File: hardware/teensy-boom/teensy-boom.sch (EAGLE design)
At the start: 5 parts

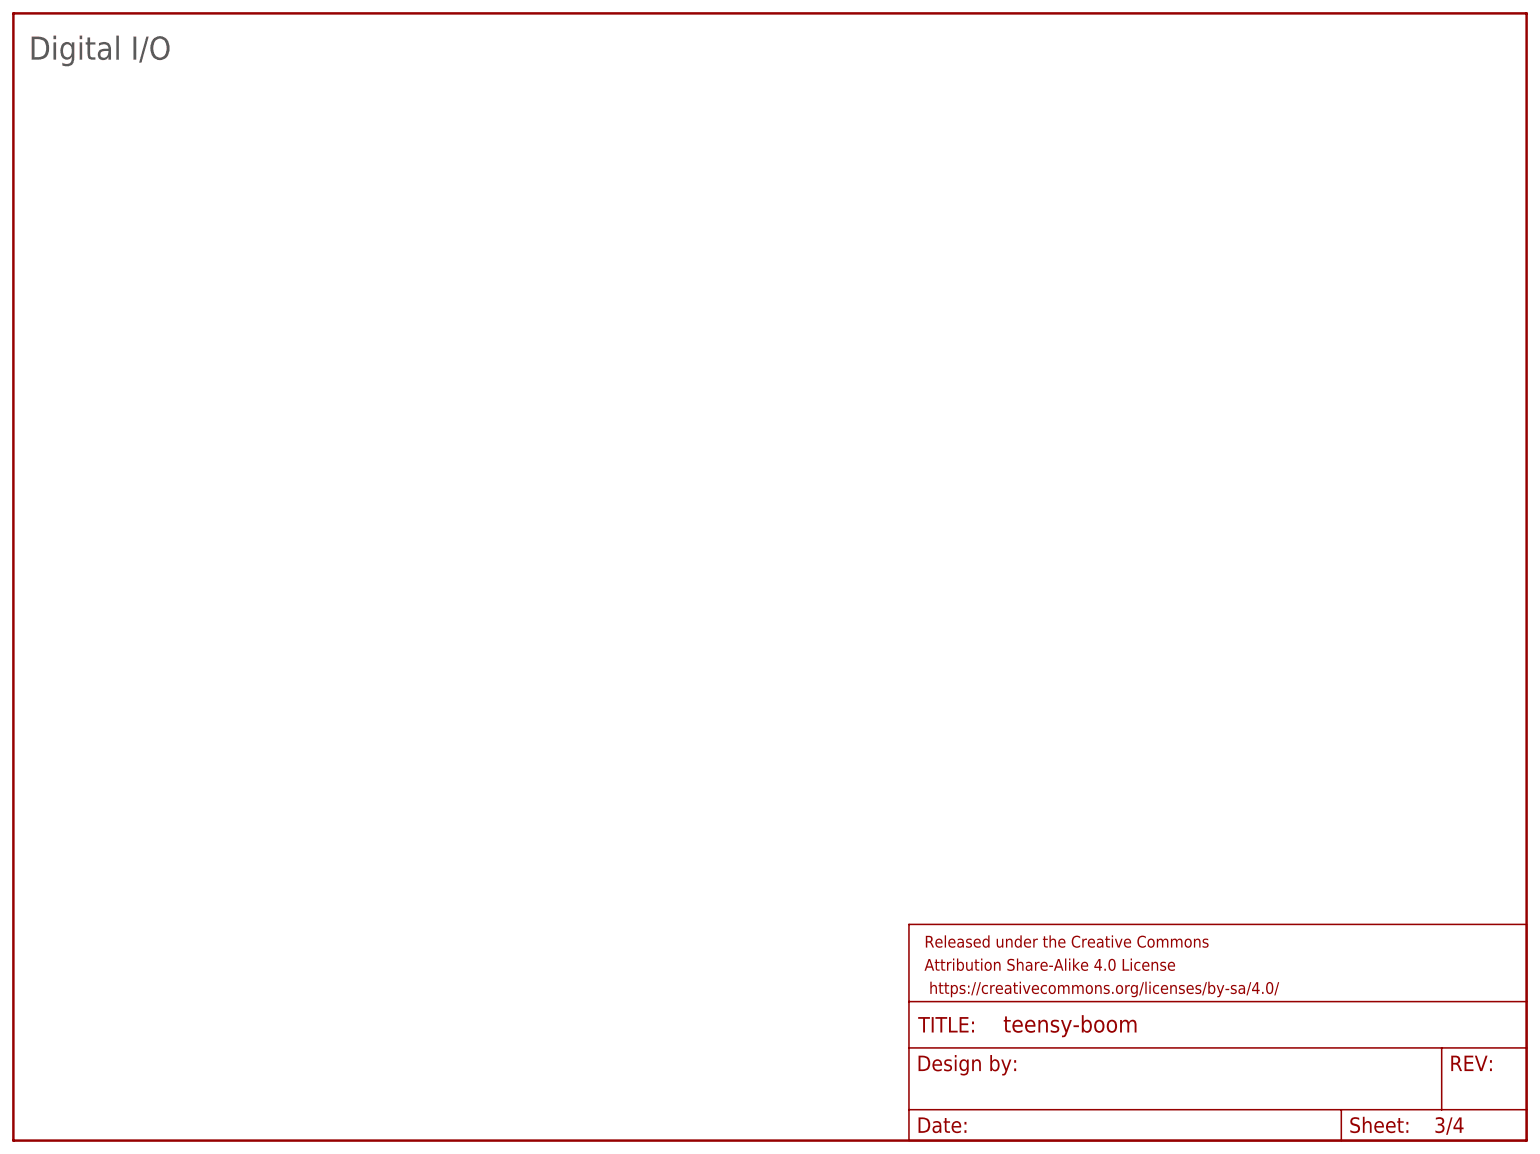
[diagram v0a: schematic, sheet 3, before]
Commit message: More PCB work
Added knobs, buttons, connectors, MIDI.

Basic PCB alignment in place...~6"x4"
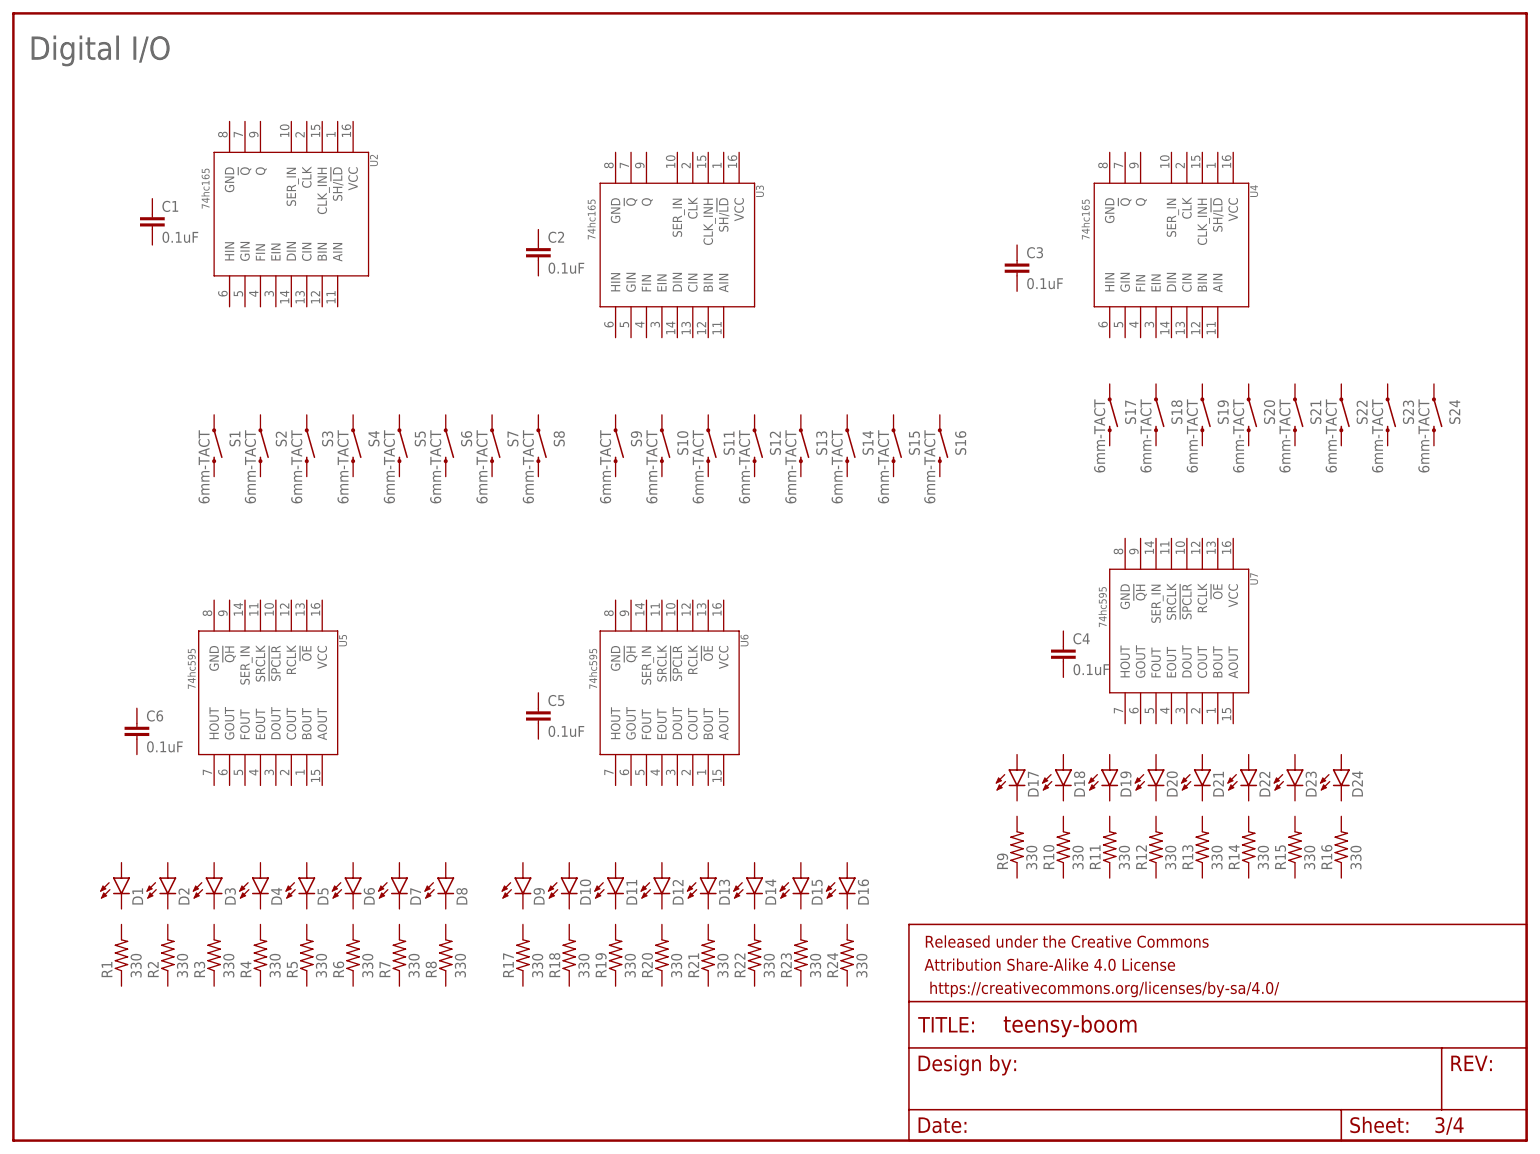
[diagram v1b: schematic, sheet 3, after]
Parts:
- added C1, C2, C3, C4, C5, C6: 0.1uF, SparkFun-Capacitors:0.1UF-25V-5%(0603)
- added D1, D10, D11, D12, D13, D14, D15, D16, D17, D18, D19, D2, D20, D21, D22, D23, D24, D3, D4, D5, D6, D7, D8, D9: (no value), SparkFun-LED:LED-3MM-NO_SILK
- added D25: MBRA140, SparkFun-DiscreteSemi:DIODE-SCHOTTKY-MBRA140
- added J1, J2, J3: AUDIO-JACK4-.25-HORIZ-TRS, SparkFun-Connectors:AUDIO-JACK4-.25-HORIZ-TRS
- added J4, J5: 5-PIN-CIRCULAR-DINNEW, Testing:5-PIN-CIRCULAR-DINNEW
- added R1, R10, R11, R12, R13, R14, R15, R16, R17, R18, R19, R2, R20, R21, R22, R23, R24, R3, R4, R5, R6, R7, R8, R9: 330, SparkFun-Resistors:330OHM1/10W1%(0603)
- added R25, R26, R27, R28: 220, SparkFun-Resistors:220OHM-1/10W-1%(0603)
- added RV1, RV10, RV11, RV12, RV13, RV14, RV2, RV3, RV4, RV5, RV6, RV7, RV8, RV9: (no value), SparkFun-Electromechanical:POTALPS-KIT
- added S1, S10, S11, S12, S13, S14, S15, S16, S17, S18, S19, S2, S20, S21, S22, S23, S24, S3, S4, S5, S6, S7, S8, S9: 6mm-TACT, SparkFun-Electromechanical:SWITCH-MOMENTARY-2PTH
- added U1: SGTL5000, teensy-synth:SGTL5000QFN-32
- added U2, U3, U4: 74hc165, teensy-synth:74HC165
- added U5, U6, U7: 74hc595, teensy-synth:74HC595
- added U8: 6N138M, SparkFun-DiscreteSemi:OPTO_DARL_6N138S
- added U9: 74AHC1G125, SparkFun-DigitalIC:74AHC1G125
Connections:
- new net 5V: R26.2, R28.2, U8.VCC, U9.VCC
- new net GND: J5.2, U8.GND, U9./OE, U9.GND
- new net N$1: U9.A
- new net N$2: J4.4, R25.1
- new net N$3: D25.C, R25.2, U8.A
- new net N$4: D25.A, J4.5, U8.C
- new net N$5: R26.1, U8.VOUT
- new net N$7: R27.1, U9.Y
- new net N$8: J5.5, R27.2
- new net N$9: J5.4, R28.1
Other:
- note added: "Cymbal"
- note added: "Decay"
- note added: "Harmony"
- note added: "Hats"
- note added: "Kick"
- note added: "Master"
- note added: "Mod-depth"
- note added: "Pitch"
- note added: "Power Supplies & MIDI"
- note added: "Snare"
- note added: "Tempo"
- note added: "Toms"
- note added: "Tone"
- note added: "Volume"
- note added: "tone/noise"
- note removed: "Power Supplies"

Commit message: More work on PCB/Schem
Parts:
- D1, D10, D11, D12, D13, D14, D15, D16, D17, D18, D19, D2, D20, D21, D22, D23, D24, D3, D4, D5, D6, D7, D8, D9: value (none) -> red
- RV1, RV10, RV11, RV12, RV13, RV14, RV2, RV3, RV4, RV5, RV6, RV7, RV8, RV9: value (none) -> 100k
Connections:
- new net AGND: RV1.A, RV10.A, RV11.A, RV12.A, RV13.A, RV14.A, RV2.A, RV3.A, RV4.A, RV5.A, RV6.A, RV7.A, RV8.A, RV9.A, SUB1EDGES.AGND, U1.AGND
- new net AREF: RV1.E, RV10.E, RV11.E, RV12.E, RV13.E, RV14.E, RV2.E, RV3.E, RV4.E, RV5.E, RV6.E, RV7.E, RV8.E, RV9.E, SUB1BACK.AREF
- new net BCLK: SUB1EDGES.9, U1.BCLK
- new net CYM-DECAY: RV11.S, SUB1BACK.27/A16
- new net CYM-MIX: RV10.S, SUB1END.A14
- new net HAT-DECAY: RV12.S, SUB1BACK.28/A17
- new net I2CRX: SUB1EDGES.13, U1.RX
- new net I2CTX: SUB1EDGES.22/A8, U1.TX
- new net KIK-DECAY: RV3.S, SUB1EDGES.17/A3
- new net KIK-MOD: RV2.S, SUB1EDGES.16/A2
- new net KIK-PITCH: RV1.S, SUB1EDGES.15/A1
- new net LRCLK: SUB1EDGES.23/A9, U1.LRCLK
- new net MCLK: SUB1EDGES.11, U1.MCLK
- new net N$10: D2.C, R2.2
- new net N$11: D3.C, R3.2
- new net N$12: D4.C, R4.2
- new net N$13: D5.C, R5.2
- new net N$14: D6.C, R6.2
- new net N$15: D7.C, R7.2
- new net N$16: D8.C, R8.2
- new net N$17: D9.C, R17.2
- new net N$18: D10.C, R18.2
- new net N$19: D11.C, R19.2
- new net N$20: D12.C, R20.2
- new net N$21: D13.C, R21.2
- new net N$22: D14.C, R22.2
- new net N$23: D15.C, R23.2
- new net N$24: D16.C, R24.2
- new net N$26: D17.C, R9.2
- new net N$27: D18.C, R10.2
- new net N$28: D19.C, R11.2
- new net N$29: D20.C, R12.2
- new net N$30: D21.C, R13.2
- new net N$31: D22.C, R14.2
- new net N$32: D23.C, R15.2
- new net N$33: D24.C, R16.2
- new net N$34: D5.A, U5.DOUT
- new net N$35: D4.A, U5.EOUT
- new net N$36: D3.A, U5.FOUT
- new net N$37: D2.A, U5.GOUT
- new net N$38: D1.A, U5.HOUT
- new net N$39: D6.A, U5.COUT
- new net N$40: D7.A, U5.BOUT
- new net N$41: D8.A, U5.AOUT
- new net N$42: D12.A, U6.EOUT
- new net N$43: D11.A, U6.FOUT
- new net N$44: D10.A, U6.GOUT
- new net N$45: D9.A, U6.HOUT
- new net N$46: D13.A, U6.DOUT
- new net N$47: D14.A, U6.COUT
- new net N$48: D15.A, U6.BOUT
- new net N$49: D16.A, U6.AOUT
- new net N$50: D20.A, U7.EOUT
- new net N$51: D19.A, U7.FOUT
- new net N$52: D18.A, U7.GOUT
- new net N$53: D17.A, U7.HOUT
- new net N$54: D21.A, U7.DOUT
- new net N$55: D24.A, U7.AOUT
- new net N$56: D23.A, U7.BOUT
- new net N$57: D22.A, U7.COUT
- new net N$6: D1.C, R1.2
- new net SCL: SUB1EDGES.19/A5, U1.SCL
- new net SDA: SUB1EDGES.18/A4, U1.SDA
- new net SNR-DECAY: RV6.S, SUB1BACK.A10
- new net SNR-MIX: RV5.S, SUB1EDGES.21/A7
- new net SNR-PITCH: RV4.S, SUB1EDGES.20/A6
- new net TEMPO: RV14.S, SUB1BACK.29/A18
- new net TOM-2ND: RV8.S, SUB1BACK.A12
- new net TOM-DECAY: RV9.S, SUB1BACK.A13
- new net TOM-PITCH: RV7.S, SUB1BACK.A11
- new net VOLUME: RV13.S, SUB1BACK.30/A19
- net GND: now also R1.1, R10.1, R11.1, R12.1, R13.1, R14.1, R15.1, R16.1, R17.1, R18.1, R19.1, R2.1, R20.1, R21.1, R22.1, R23.1, R24.1, R3.1, R4.1, R5.1, R6.1, R7.1, R8.1, R9.1, SUB1BACK.GND, SUB1EDGES.GND, SUB1END.GND, U1.ADDR, U1.GND@1, U1.GND@3, U1.GND@PAD, U1.MODE
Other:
- moved on the sheet: C4, U7

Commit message: More work on BOOM schem/PCB.
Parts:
- removed C4, C5, C6: 0.1uF, SparkFun-Capacitors:0.1UF-25V-5%(0603)
- added C10, C7, C8, C9: 2.2uF, SparkFun-Capacitors:2.2UF-25V-+80/-20(0805)
- added C11: 0.1u, SparkFun-Capacitors:CAP0805
- added C12, C13, C14: 0.1uF, SparkFun-Capacitors:0.1UF-25V-5%(0603)
- added FRAME5: FRAME-LETTERNO_PACKAGE, SparkFun-Aesthetics:FRAME-LETTERNO_PACKAGE
- added J6: Inputs, SparkFun-Connectors:M03LOCK
- added R29, R30, R31, R32, R33, R34, R35, R36, R37, R38, R39, R40, R41, R42, R43, R44, R45, R46, R47, R48, R49, R50, R51, R52: 100k, SparkFun-Resistors:RESISTOR0805-RES
- J1: value AUDIO-JACK4-.25-HORIZ-TRS -> LEFT-OUT
- J2: value AUDIO-JACK4-.25-HORIZ-TRS -> RIGHT-OUT
- J3: value AUDIO-JACK4-.25-HORIZ-TRS -> PHONES
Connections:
- new net 3.3V: C1.1, C12.1, C13.1, C14.1, C2.1, C3.1, R29.2, R30.2, R31.2, R32.2, R33.2, R34.2, R35.2, R36.2, R37.2, R38.2, R39.2, R40.2, R41.2, R42.2, R43.2, R44.2, R45.2, R46.2, R47.2, R48.2, R49.2, R50.2, R51.2, R52.2, U2.VCC, U3.VCC, U4.VCC, U5.VCC, U6.VCC, U7.VCC
- new net N$25: C8.1, J2.TIP
- new net N$58: C7.2, J1.TIP
- new net N$59: C8.2, U1.LINEOUTR
- new net N$60: C7.1, U1.LINEOUTL
- new net N$61: C10.2, U1.LINEINR
- new net N$62: C9.2, U1.LINEINL
- new net N$63: J3.TIP, U1.HPL
- new net N$64: J3.RING, U1.HPR
- new net N$65: J3.EARTH, U1.HPGND
- new net N$66: C9.1, J6.2
- new net N$67: C10.1, J6.3
- new net N$68: C11.1, U1.VAG
- new net N$69: R35.1, S7.1, U2.GIN
- new net N$70: R29.1, S1.1, U2.AIN
- new net N$71: R30.1, S2.1, U2.BIN
- new net N$72: R31.1, S3.1, U2.CIN
- new net N$73: R32.1, S4.1, U2.DIN
- new net N$74: R33.1, S5.1, U2.EIN
- new net N$75: R34.1, S6.1, U2.FIN
- new net N$76: R36.1, S8.1, U2.HIN
- new net N$77: R37.1, S9.1, U3.AIN
- new net N$78: R38.1, S10.1, U3.BIN
- new net N$79: R39.1, S11.1, U3.CIN
- new net N$80: R40.1, S12.1, U3.DIN
- new net N$81: R41.1, S13.1, U3.EIN
- new net N$82: R42.1, S14.1, U3.FIN
- new net N$83: R43.1, S15.1, U3.GIN
- new net N$84: R44.1, S16.1, U3.HIN
- new net N$840: R52.1, S24.1, U4.HIN
- new net N$85: R45.1, S17.1, U4.AIN
- new net N$86: R46.1, S18.1, U4.BIN
- new net N$87: R47.1, S19.1, U4.CIN
- new net N$88: R48.1, S20.1, U4.DIN
- new net N$89: R49.1, S21.1, U4.EIN
- new net N$90: R50.1, S22.1, U4.FIN
- new net N$91: R51.1, S23.1, U4.GIN
- net AGND: now also J1.EARTH, J2.EARTH, J6.1
- net GND: now also C1.2, C11.2, C12.2, C13.2, C14.2, C2.2, C3.2, S1.2, S10.2, S11.2, S12.2, S13.2, S14.2, S15.2, S16.2, S17.2, S18.2, S19.2, S2.2, S20.2, S21.2, S22.2, S23.2, S24.2, S3.2, S4.2, S5.2, S6.2, S7.2, S8.2, S9.2, U2.GND, U3.GND, U4.GND, U5.GND, U6.GND, U7.GND

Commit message: Checking in WIP of large Teensy-BOOM board, so I can move to smaller one.
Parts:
- added C15, C5: 10uF, SparkFun-Capacitors:10UF-6.3V-20%(0603)
- added C16: 2.2uF, SparkFun-Capacitors:2.2UF-25V-+80/-20(0805)
- added C4, C48, C6: 0.1uF, SparkFun-Capacitors:0.1UF-25V(+80/-20%)(0603)
- added D26, D27: MBRA140, SparkFun-DiscreteSemi:DIODE-SCHOTTKY-MBRA140
- added FD1, FD2: FIDUCIALUFIDUCIAL, SparkFun-Aesthetics:FIDUCIALUFIDUCIAL
- added H1, H2, H3, H4, H5, H6: STAND-OFF, SparkFun-Electromechanical:STAND-OFF
- added J10: 3.3V, SparkFun-Passives:TEST-POINTTP_15TH_THRU
- added J11: VIN, SparkFun-Passives:TEST-POINTTP_15TH_THRU
- added J7: POWER_JACKPTH_LOCK, SparkFun-Connectors:POWER_JACKPTH_LOCK
- added J9: 1.8V, SparkFun-Passives:TEST-POINTTP_15TH_THRU
- added R53: 105, SparkFun-Resistors:105OHM-1/10W-1%(0603)
- added R54: 240, SparkFun-Resistors:240OHM1/10W1%(0603)
- added R55, R56: 390, SparkFun-Resistors:390OHM1/10W1%(0603)
- added R57, R58: 2.2k, SparkFun-Resistors:2.2KOHM-1/10W-1%(0603)
- added U10, U11: LM1117, SparkFun-PowerIC:V_REG_LM1117SOT223
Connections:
- new net 1.8V: C5.1, J9.1, R53.2, U1.VDDD, U10.OUT, U10.OUT@1
- new net N$100: U3.Q, U4.SER_IN
- new net N$92: U5.!QH, U6.SER_IN
- new net N$93: C4.1, C6.1, D26.C, D27.C, U10.IN, U11.IN
- new net N$94: R53.1, R55.2, U10.ADJ
- new net N$95: R54.1, R56.2, U11.ADJ
- new net N$96: SUB1EDGES.10
- new net N$97: C16.1, C48.1, U1.VDDA
- new net N$98: U6.!QH, U7.SER_IN
- new net N$99: U2.Q, U3.SER_IN
- new net SPI-CLK: SUB1EDGES.14/A0, U2.CLK, U5.SRCLK
- new net SPI-MISO: SUB1EDGES.12, U4.Q
- new net SPI-MOSI: SUB1EDGES.7, U5.SER_IN
- new net VIN: D27.A, J11.1, J7.PWR
- new net VUSB: D26.A, SUB1BACK.VUSB
- net 3.3V: now also C15.1, J10.1, R54.2, R57.2, R58.2, U1.VDDIO, U11.OUT, U11.OUT@1, U5.!SPCLR, U6.!SPCLR, U7.!SPCLR
- net GND: now also C15.2, C16.2, C4.2, C48.2, C5.2, C6.2, J7.GND, J7.GNDBREAK, R55.1, R56.1, U2.CLK_INH, U3.CLK_INH, U4.CLK_INH, U5.!OE, U6.!OE, U7.!OE
- net SCL: now also R58.1
- net SDA: now also R57.1
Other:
- note added: "165 Notes: Inhibit disables clock - not useful here SH/!LD is effectively CS"
- note added: "595 Notes: RCLK is output latch strobe, active Hi. SRCLK is data shift clock, sampled on rising edge. !SPCLR chears shift register. !QH is shift data out"
- note added: "Digital I/O: LEDs"
- note added: "Vin range: 5 to 15 VDC"
- moved on the sheet: C1, C12, C13, C14, C2, C3, D1, D10, D11, D12, D13, D14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
